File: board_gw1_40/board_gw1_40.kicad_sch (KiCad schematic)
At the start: 214 parts, among them J1 USB_C_Receptacle, Q1 2N7002, Q10 2N7002, Q11 2N7002, Q12 2N7002, Q13 2N7002, Q14 2N7002, Q15 2N7002, Q16 2N7002, Q17 2N7002, Q18 2N7002, Q19 2N7002, Q2 2N7002, Q20 2N7002, Q21 2N7002, Q22 2N7002, Q23 2N7002, Q24 2N7002, Q25 2N7002, Q26 2N7002, Q27 2N7002, Q28 2N7002, Q29 2N7002, Q3 2N7002, Q30 2N7002, Q31 2N7002, Q32 2N7002, Q33 2N7002, Q34 2N7002, Q35 2N7002, Q36 2N7002, Q37 2N7002, Q38 2N7002, Q39 2N7002, Q4 2N7002, Q40 2N7002, Q41 2N7002, Q5 2N7002, Q6 2N7002, Q7 2N7002, Q8 2N7002, Q9 2N7002, U1 GW1NR-LV9-QN88-C6/I5, U11 FT232H, U2 ESD224DQA, U3 MIC5203-3.3BM5, U4 APS6404L-3SQR-ZR, U5 MIC5504-1.2YM5, U6 TPS562242, U7 W25Q16JVUXIQ, X2 27MHz, Y1 12MHz

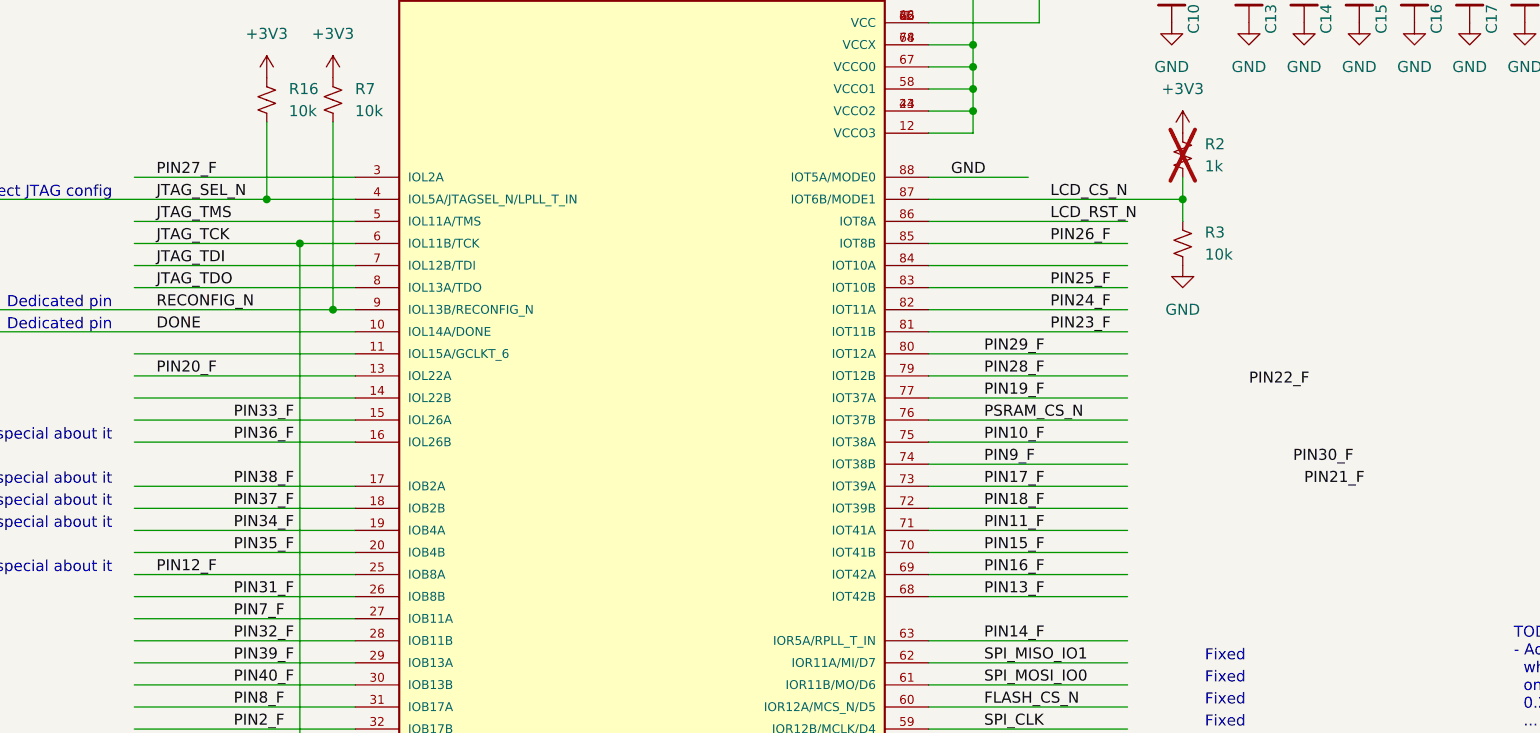
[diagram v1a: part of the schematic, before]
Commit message: Some progress on 40-pin USB
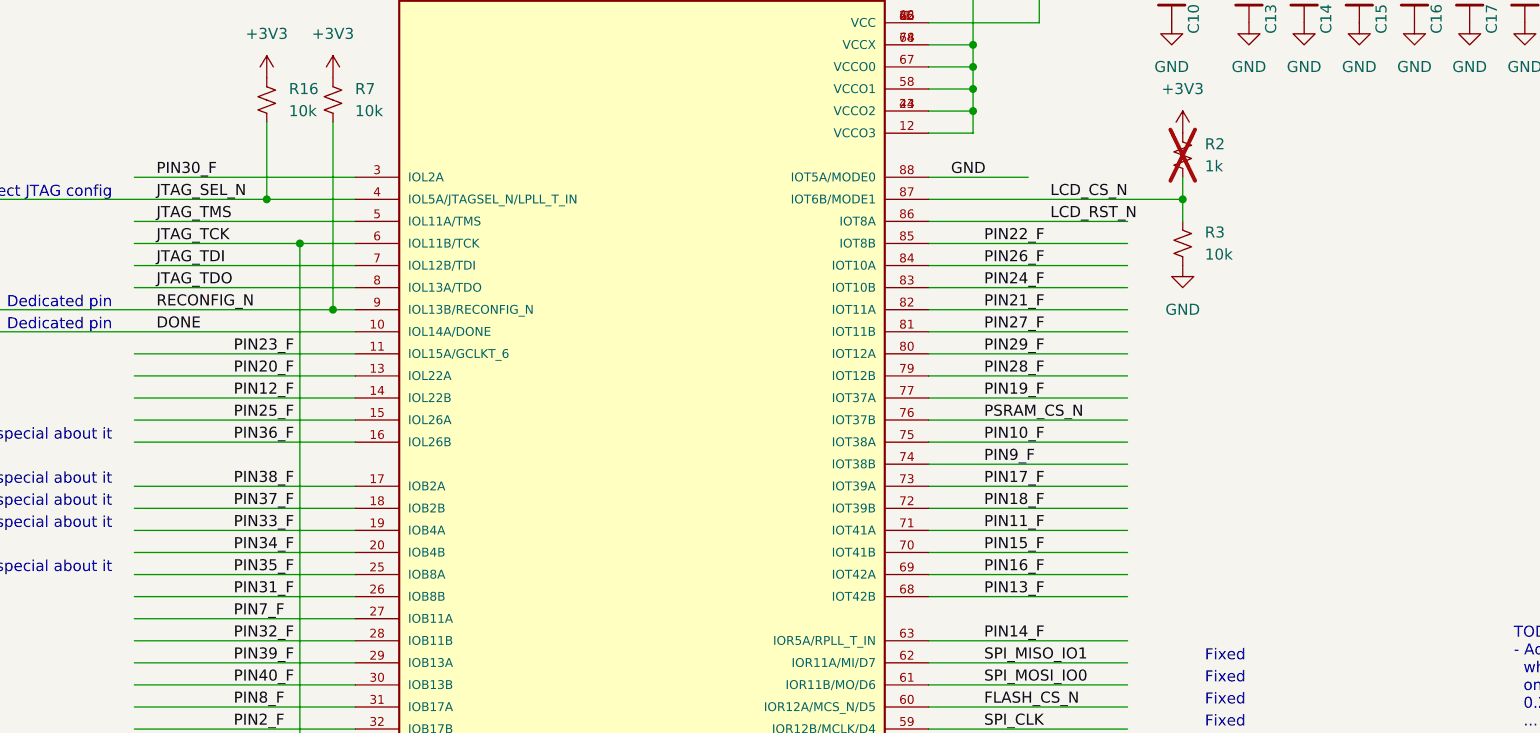
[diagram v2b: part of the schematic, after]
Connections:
- net PIN12_F: now also U1.14 (IOL22B); no longer U1.25 (IOB8A)
- net PIN21_F: now also U1.82 (IOT11A)
- net PIN22_F: now also U1.85 (IOT8B)
- net PIN23_F: now also U1.11 (IOL15A/GCLKT_6); no longer U1.81 (IOT11B)
- net PIN24_F: now also U1.83 (IOT10B); no longer U1.82 (IOT11A)
- net PIN25_F: now also U1.15 (IOL26A); no longer U1.83 (IOT10B)
- net PIN26_F: now also U1.84 (IOT10A); no longer U1.85 (IOT8B)
- net PIN27_F: now also U1.81 (IOT11B); no longer U1.3 (IOL2A)
- net PIN30_F: now also U1.3 (IOL2A)
- net PIN33_F: now also U1.19 (IOB4A); no longer U1.15 (IOL26A)
- net PIN34_F: now also U1.20 (IOB4B); no longer U1.19 (IOB4A)
- net PIN35_F: now also U1.25 (IOB8A); no longer U1.20 (IOB4B)
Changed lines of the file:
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@@
 	)
 	(label "PIN23_F"
-		(at 182.88 85.09 0)
+		(at 88.9 87.63 0)
 		(effects
 			(font
@@
 	)
 	(label "PIN26_F"
-		(at 182.88 74.93 0)
+		(at 175.26 77.47 0)
 		(effects
 			(font
@@
 	)
 	(label "PIN12_F"
-		(at 80.01 113.03 0)
+		(at 88.9 92.71 0)
 		(effects
 			(font
@@
 	)
 	(label "PIN22_F"
-		(at 205.74 91.44 0)
+		(at 175.26 74.93 0)
 		(effects
 			(font
@@
 	)
 	(label "PIN24_F"
-		(at 182.88 82.55 0)
+		(at 175.26 80.01 0)
 		(effects
 			(font
@@
 	)
 	(label "PIN30_F"
-		(at 210.82 100.33 0)
+		(at 80.01 67.31 0)
 		(effects
 			(font
@@
 	)
 	(label "PIN20_F"
-		(at 80.01 90.17 0)
+		(at 88.9 90.17 0)
 		(effects
 			(font
@@
 	)
 	(label "PIN33_F"
-		(at 88.9 95.25 0)
+		(at 88.9 107.95 0)
 		(effects
 			(font
@@
 	)
 	(label "PIN27_F"
-		(at 80.01 67.31 0)
+		(at 175.26 85.09 0)
 		(effects
 			(font
@@
 	)
 	(label "PIN34_F"
-		(at 88.9 107.95 0)
+		(at 88.9 110.49 0)
 		(effects
 			(font
@@
 	)
 	(label "PIN35_F"
-		(at 88.9 110.49 0)
+		(at 88.9 113.03 0)
 		(effects
 			(font
@@
 	)
 	(label "PIN21_F"
-		(at 212.09 102.87 0)
+		(at 175.26 82.55 0)
 		(effects
 			(font
@@
 	)
 	(label "PIN25_F"
-		(at 182.88 80.01 0)
-		(effects
-			(font
+		(at 88.9 95.25 0)
+		(effects
+			(font
